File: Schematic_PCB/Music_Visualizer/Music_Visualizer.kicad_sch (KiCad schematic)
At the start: 145 parts, among them J1 AudioJack3, J3 Screw_Terminal_01x02, SW1 SW_SPDT, U1 LM324, U2 LM324, U3 LM324, U4 LM324, U5 LM324, U6 LM324, U7 LM324

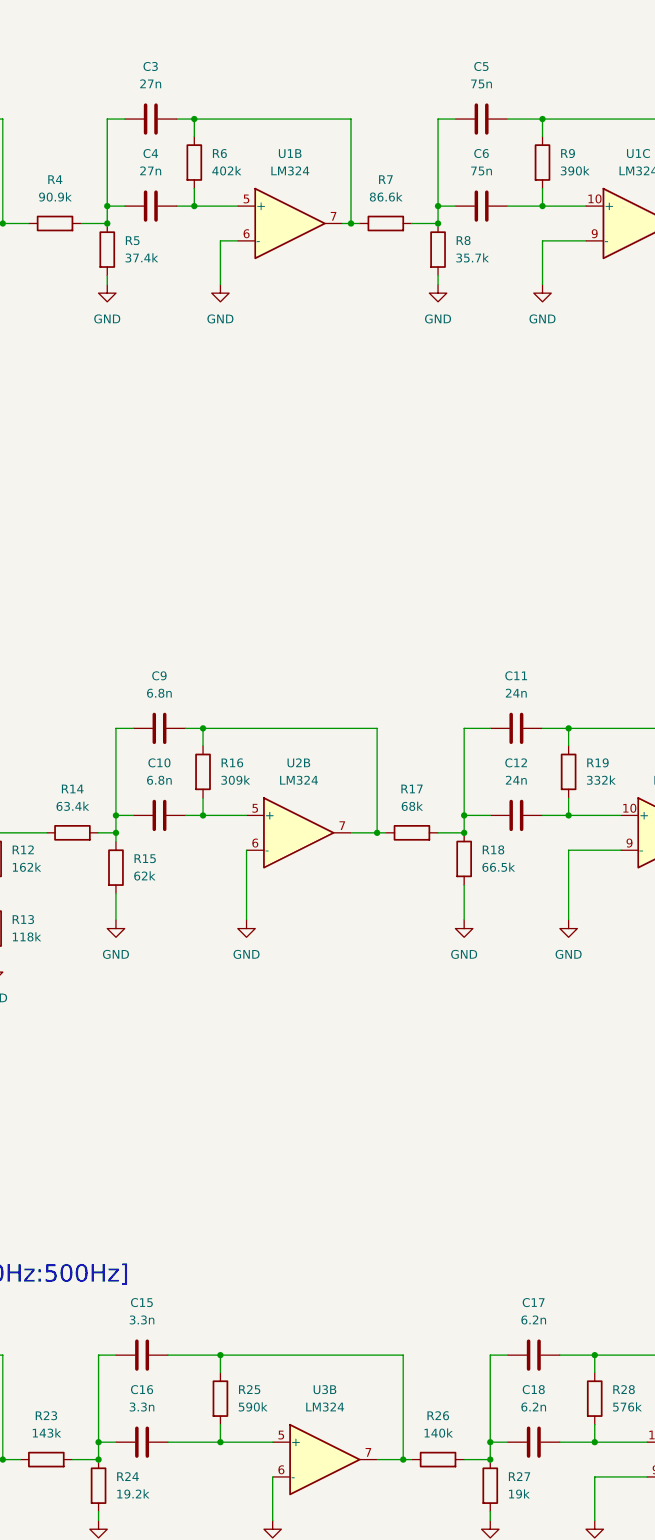
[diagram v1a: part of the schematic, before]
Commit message: Started sourcing parts from digikey, got to part 15, corrected mistakes as I go along
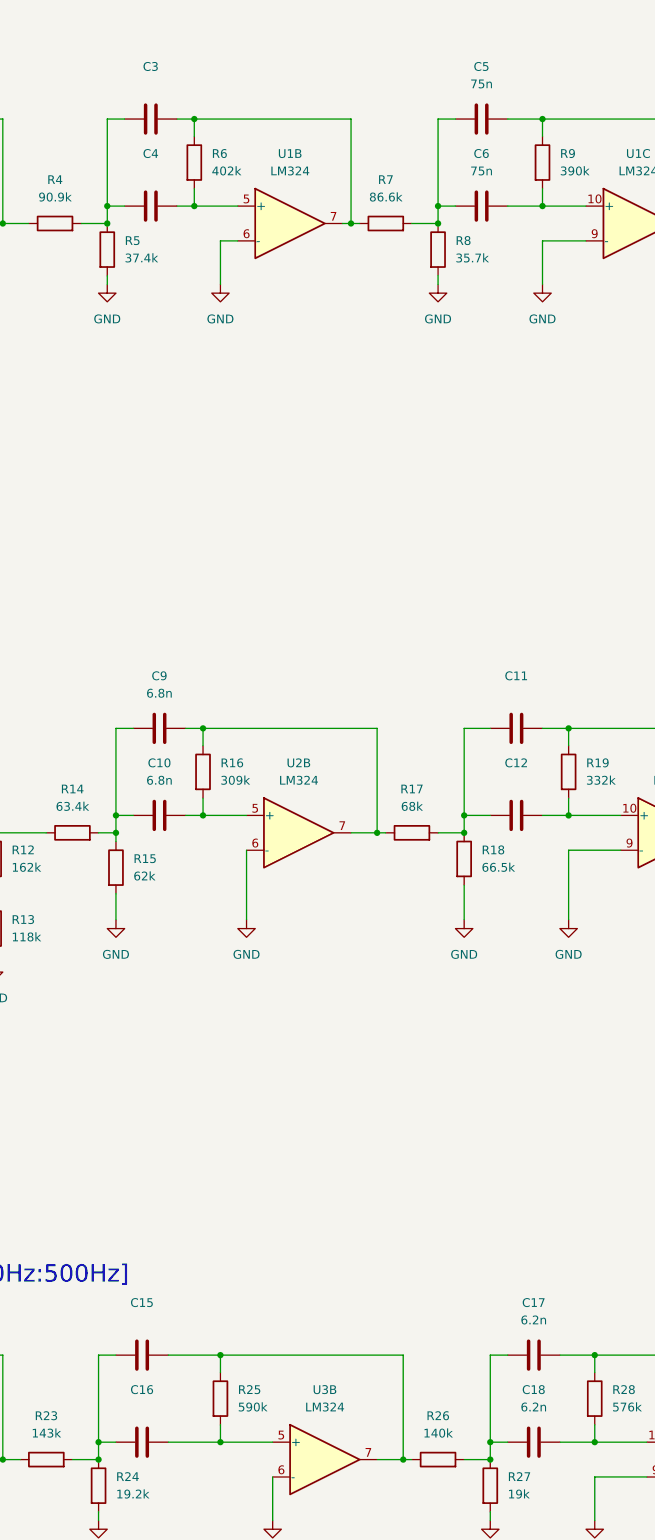
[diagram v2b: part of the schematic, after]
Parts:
- C11, C12: value 24n -> (none); footprint Capacitor_SMD:C_1206_3216Metric -> (none)
- C15, C16: value 3.3n -> (none); footprint Capacitor_SMD:C_0402_1005Metric -> (none)
- C3, C4: value 27n -> (none); footprint Capacitor_SMD:C_0402_1005Metric -> (none)
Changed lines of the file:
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@@
     (in_bom yes) (on_board yes) (fields_autoplaced)
     (property "Reference" "C11" (id 0) (at 189.23 116.84 90))
-    (property "Value" "24n" (id 1) (at 189.23 119.38 90))
-    (property "Footprint" "Capacitor_SMD:C_1206_3216Metric" (id 2) (at 193.04 123.4948 0)
+    (property "Value" "" (id 1) (at 189.23 119.38 90))
+    (property "Footprint" "" (id 2) (at 193.04 123.4948 0)
       (effects (font (size 1.27 1.27)) hide)
     )
@@
     (in_bom yes) (on_board yes) (fields_autoplaced)
     (property "Reference" "C12" (id 0) (at 189.23 129.54 90))
-    (property "Value" "24n" (id 1) (at 189.23 132.08 90))
-    (property "Footprint" "Capacitor_SMD:C_1206_3216Metric" (id 2) (at 193.04 136.1948 0)
+    (property "Value" "" (id 1) (at 189.23 132.08 90))
+    (property "Footprint" "" (id 2) (at 193.04 136.1948 0)
       (effects (font (size 1.27 1.27)) hide)
     )
@@
     (in_bom yes) (on_board yes) (fields_autoplaced)
     (property "Reference" "C15" (id 0) (at 134.62 208.28 90))
-    (property "Value" "3.3n" (id 1) (at 134.62 210.82 90))
-    (property "Footprint" "Capacitor_SMD:C_0402_1005Metric" (id 2) (at 138.43 214.9348 0)
+    (property "Value" "" (id 1) (at 134.62 210.82 90))
+    (property "Footprint" "" (id 2) (at 138.43 214.9348 0)
       (effects (font (size 1.27 1.27)) hide)
     )
@@
     (in_bom yes) (on_board yes) (fields_autoplaced)
     (property "Reference" "C4" (id 0) (at 135.89 40.64 90))
-    (property "Value" "27n" (id 1) (at 135.89 43.18 90))
-    (property "Footprint" "Capacitor_SMD:C_0402_1005Metric" (id 2) (at 139.7 47.2948 0)
+    (property "Value" "" (id 1) (at 135.89 43.18 90))
+    (property "Footprint" "" (id 2) (at 139.7 47.2948 0)
       (effects (font (size 1.27 1.27)) hide)
     )
@@
     (in_bom yes) (on_board yes)
     (property "Reference" "C3" (id 0) (at 135.89 27.94 90))
-    (property "Value" "27n" (id 1) (at 135.89 30.48 90))
-    (property "Footprint" "Capacitor_SMD:C_0402_1005Metric" (id 2) (at 139.7 34.5948 0)
+    (property "Value" "" (id 1) (at 135.89 30.48 90))
+    (property "Footprint" "" (id 2) (at 139.7 34.5948 0)
       (effects (font (size 1.27 1.27)) hide)
     )
@@
     (in_bom yes) (on_board yes) (fields_autoplaced)
     (property "Reference" "C16" (id 0) (at 134.62 220.98 90))
-    (property "Value" "3.3n" (id 1) (at 134.62 223.52 90))
-    (property "Footprint" "Capacitor_SMD:C_0402_1005Metric" (id 2) (at 138.43 227.6348 0)
+    (property "Value" "" (id 1) (at 134.62 223.52 90))
+    (property "Footprint" "" (id 2) (at 138.43 227.6348 0)
       (effects (font (size 1.27 1.27)) hide)
     )
@@
     )
     (path "/9bf0cba7-9517-4cba-992a-c8ed29af4729"
-      (reference "C3") (unit 1) (value "27n") (footprint "Capacitor_SMD:C_0402_1005Metric")
+      (reference "C3") (unit 1) (value "27n") (footprint "Capacitor_SMD:C_0603_1608Metric")
     )
     (path "/8c47b6ff-34b1-402d-a1f0-32ec90f1ac1e"
-      (reference "C4") (unit 1) (value "27n") (footprint "Capacitor_SMD:C_0402_1005Metric")
+      (reference "C4") (unit 1) (value "27n") (footprint "Capacitor_SMD:C_0603_1608Metric")
     )
     (path "/77886ef4-a79a-47d1-b490-9ff1ad540d06"
@@
     )
     (path "/090684f0-2db5-4c27-adcd-136c105cb53b"
-      (reference "C11") (unit 1) (value "24n") (footprint "Capacitor_SMD:C_1206_3216Metric")
+      (reference "C11") (unit 1) (value "24n") (footprint "Capacitor_SMD:C_0805_2012Metric")
     )
     (path "/2a2a8a1f-a295-45d5-9418-ae650bcb2e29"
-      (reference "C12") (unit 1) (value "24n") (footprint "Capacitor_SMD:C_1206_3216Metric")
+      (reference "C12") (unit 1) (value "24n") (footprint "Capacitor_SMD:C_0805_2012Metric")
     )
     (path "/20700322-fdbb-423a-a695-59bcf586eb75"
@@
     )
     (path "/79e9dcc8-186f-4c45-a5c4-64194af1b0b7"
-      (reference "C15") (unit 1) (value "3.3n") (footprint "Capacitor_SMD:C_0402_1005Metric")
+      (reference "C15") (unit 1) (value "3.3n") (footprint "Capacitor_SMD:C_0201_0603Metric")
     )
     (path "/fa3632db-5db7-41c9-81a2-0fd4b3e31b83"
-      (reference "C16") (unit 1) (value "3.3n") (footprint "Capacitor_SMD:C_0402_1005Metric")
+      (reference "C16") (unit 1) (value "3.3n") (footprint "Capacitor_SMD:C_0201_0603Metric")
     )
     (path "/35d17c18-0872-4b14-af92-9b4e4ed99599"

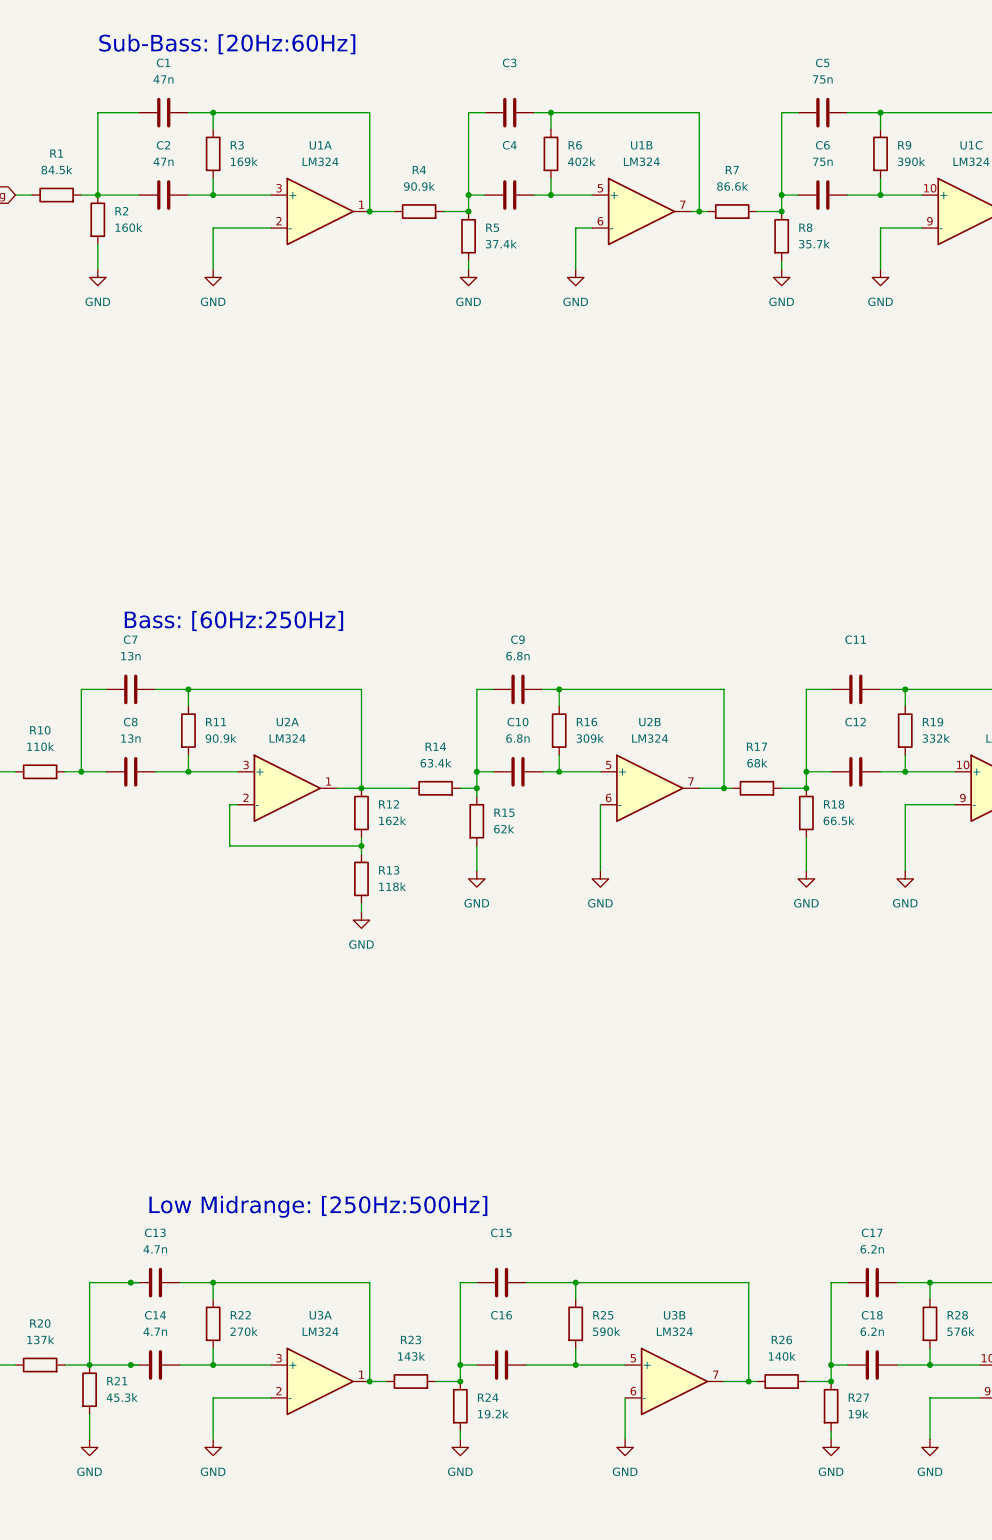
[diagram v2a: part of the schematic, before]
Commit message: Finished digi-key BOM and made appropriate changes to schematic and PCB
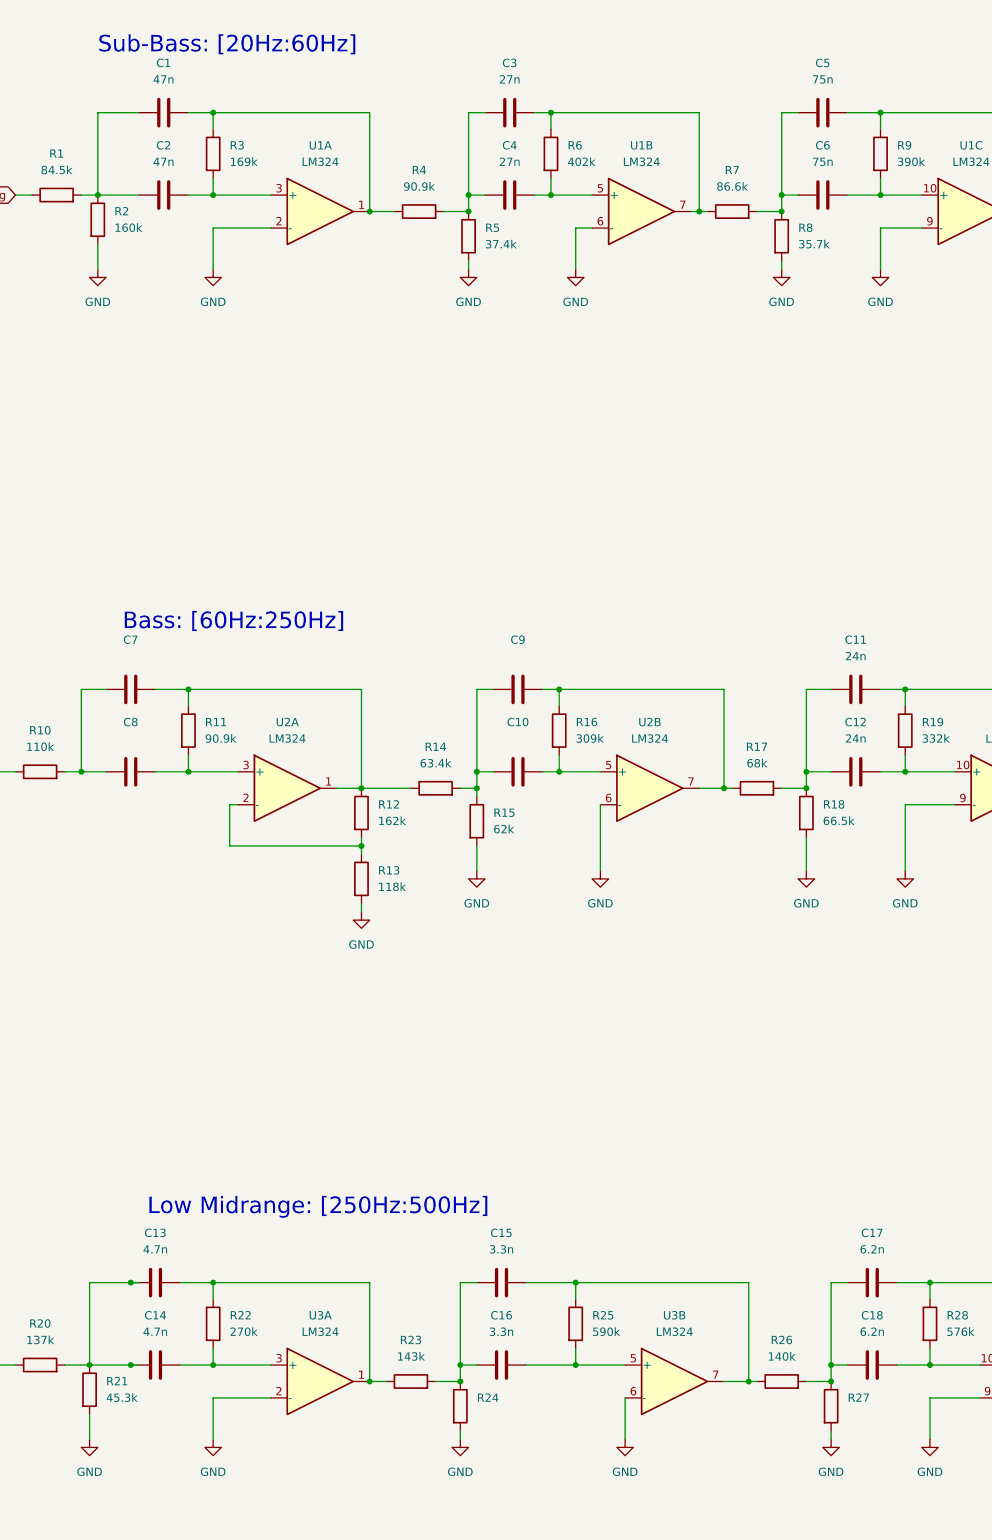
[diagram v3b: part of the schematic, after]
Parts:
- C10, C9: value 6.8n -> (none); footprint Capacitor_SMD:C_0201_0603Metric -> (none)
- C11, C12: value (none) -> 24n; footprint (none) -> Capacitor_SMD:C_0805_2012Metric
- C15, C16: value (none) -> 3.3n; footprint (none) -> Capacitor_SMD:C_0201_0603Metric
- C3, C4: value (none) -> 27n; footprint (none) -> Capacitor_SMD:C_0603_1608Metric
- C7, C8: value 13n -> (none); footprint Capacitor_SMD:C_0402_1005Metric -> (none)
- R24: value 19.2k -> (none)
- R27: value 19k -> (none)
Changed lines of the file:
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@@
     (in_bom yes) (on_board yes) (fields_autoplaced)
     (property "Reference" "C7" (id 0) (at 77.47 116.84 90))
-    (property "Value" "13n" (id 1) (at 77.47 119.38 90))
-    (property "Footprint" "Capacitor_SMD:C_0402_1005Metric" (id 2) (at 81.28 123.4948 0)
+    (property "Value" "" (id 1) (at 77.47 119.38 90))
+    (property "Footprint" "" (id 2) (at 81.28 123.4948 0)
       (effects (font (size 1.27 1.27)) hide)
     )
@@
     (in_bom yes) (on_board yes) (fields_autoplaced)
     (property "Reference" "C11" (id 0) (at 189.23 116.84 90))
-    (property "Value" "" (id 1) (at 189.23 119.38 90))
-    (property "Footprint" "" (id 2) (at 193.04 123.4948 0)
+    (property "Value" "24n" (id 1) (at 189.23 119.38 90))
+    (property "Footprint" "Capacitor_SMD:C_0805_2012Metric" (id 2) (at 193.04 123.4948 0)
       (effects (font (size 1.27 1.27)) hide)
     )
@@
       (effects (font (size 1.27 1.27)) (justify left))
     )
-    (property "Value" "19.2k" (id 1) (at 130.81 236.2199 0)
+    (property "Value" "" (id 1) (at 130.81 236.2199 0)
       (effects (font (size 1.27 1.27)) (justify left))
     )
@@
     (in_bom yes) (on_board yes) (fields_autoplaced)
     (property "Reference" "C12" (id 0) (at 189.23 129.54 90))
-    (property "Value" "" (id 1) (at 189.23 132.08 90))
-    (property "Footprint" "" (id 2) (at 193.04 136.1948 0)
+    (property "Value" "24n" (id 1) (at 189.23 132.08 90))
+    (property "Footprint" "Capacitor_SMD:C_0805_2012Metric" (id 2) (at 193.04 136.1948 0)
       (effects (font (size 1.27 1.27)) hide)
     )
@@
     (in_bom yes) (on_board yes) (fields_autoplaced)
     (property "Reference" "C10" (id 0) (at 137.16 129.54 90))
-    (property "Value" "6.8n" (id 1) (at 137.16 132.08 90))
-    (property "Footprint" "Capacitor_SMD:C_0201_0603Metric" (id 2) (at 140.97 136.1948 0)
+    (property "Value" "" (id 1) (at 137.16 132.08 90))
+    (property "Footprint" "" (id 2) (at 140.97 136.1948 0)
       (effects (font (size 1.27 1.27)) hide)
     )
@@
     (in_bom yes) (on_board yes) (fields_autoplaced)
     (property "Reference" "C15" (id 0) (at 134.62 208.28 90))
-    (property "Value" "" (id 1) (at 134.62 210.82 90))
-    (property "Footprint" "" (id 2) (at 138.43 214.9348 0)
+    (property "Value" "3.3n" (id 1) (at 134.62 210.82 90))
+    (property "Footprint" "Capacitor_SMD:C_0201_0603Metric" (id 2) (at 138.43 214.9348 0)
       (effects (font (size 1.27 1.27)) hide)
     )
@@
     (in_bom yes) (on_board yes) (fields_autoplaced)
     (property "Reference" "C9" (id 0) (at 137.16 116.84 90))
-    (property "Value" "6.8n" (id 1) (at 137.16 119.38 90))
-    (property "Footprint" "Capacitor_SMD:C_0201_0603Metric" (id 2) (at 140.97 123.4948 0)
+    (property "Value" "" (id 1) (at 137.16 119.38 90))
+    (property "Footprint" "" (id 2) (at 140.97 123.4948 0)
       (effects (font (size 1.27 1.27)) hide)
     )
@@
     (in_bom yes) (on_board yes) (fields_autoplaced)
     (property "Reference" "C4" (id 0) (at 135.89 40.64 90))
-    (property "Value" "" (id 1) (at 135.89 43.18 90))
-    (property "Footprint" "" (id 2) (at 139.7 47.2948 0)
+    (property "Value" "27n" (id 1) (at 135.89 43.18 90))
+    (property "Footprint" "Capacitor_SMD:C_0603_1608Metric" (id 2) (at 139.7 47.2948 0)
       (effects (font (size 1.27 1.27)) hide)
     )
@@
     (in_bom yes) (on_board yes)
     (property "Reference" "C3" (id 0) (at 135.89 27.94 90))
-    (property "Value" "" (id 1) (at 135.89 30.48 90))
-    (property "Footprint" "" (id 2) (at 139.7 34.5948 0)
+    (property "Value" "27n" (id 1) (at 135.89 30.48 90))
+    (property "Footprint" "Capacitor_SMD:C_0603_1608Metric" (id 2) (at 139.7 34.5948 0)
       (effects (font (size 1.27 1.27)) hide)
     )
@@
       (effects (font (size 1.27 1.27)) (justify left))
     )
-    (property "Value" "19k" (id 1) (at 187.96 236.2199 0)
+    (property "Value" "" (id 1) (at 187.96 236.2199 0)
       (effects (font (size 1.27 1.27)) (justify left))
     )
@@
     (in_bom yes) (on_board yes) (fields_autoplaced)
     (property "Reference" "C8" (id 0) (at 77.47 129.54 90))
-    (property "Value" "13n" (id 1) (at 77.47 132.08 90))
-    (property "Footprint" "Capacitor_SMD:C_0402_1005Metric" (id 2) (at 81.28 136.1948 0)
+    (property "Value" "" (id 1) (at 77.47 132.08 90))
+    (property "Footprint" "" (id 2) (at 81.28 136.1948 0)
       (effects (font (size 1.27 1.27)) hide)
     )
@@
     (in_bom yes) (on_board yes) (fields_autoplaced)
     (property "Reference" "C16" (id 0) (at 134.62 220.98 90))
-    (property "Value" "" (id 1) (at 134.62 223.52 90))
-    (property "Footprint" "" (id 2) (at 138.43 227.6348 0)
+    (property "Value" "3.3n" (id 1) (at 134.62 223.52 90))
+    (property "Footprint" "Capacitor_SMD:C_0201_0603Metric" (id 2) (at 138.43 227.6348 0)
       (effects (font (size 1.27 1.27)) hide)
     )
@@
     )
     (path "/07ee7e0f-2985-4d61-9b50-269fb321160d"
-      (reference "C7") (unit 1) (value "13n") (footprint "Capacitor_SMD:C_0402_1005Metric")
+      (reference "C7") (unit 1) (value "13n") (footprint "Capacitor_SMD:C_0805_2012Metric")
     )
     (path "/f487e740-61ea-48e8-a052-40ab7e8322a0"
-      (reference "C8") (unit 1) (value "13n") (footprint "Capacitor_SMD:C_0402_1005Metric")
+      (reference "C8") (unit 1) (value "13n") (footprint "Capacitor_SMD:C_0805_2012Metric")
     )
     (path "/83d23cec-73ff-46df-90f0-af0a3e52ad46"
-      (reference "C9") (unit 1) (value "6.8n") (footprint "Capacitor_SMD:C_0201_0603Metric")
+      (reference "C9") (unit 1) (value "6.8n") (footprint "Capacitor_SMD:C_0805_2012Metric")
     )
     (path "/671fc4a8-8b88-4bcb-9c54-7c1fba0aad0e"
-      (reference "C10") (unit 1) (value "6.8n") (footprint "Capacitor_SMD:C_0201_0603Metric")
+      (reference "C10") (unit 1) (value "6.8n") (footprint "Capacitor_SMD:C_0805_2012Metric")
     )
     (path "/090684f0-2db5-4c27-adcd-136c105cb53b"
@@
     )
     (path "/24620dcc-52e7-4176-bbe7-843dfe8a0615"
-      (reference "R24") (unit 1) (value "19.2k") (footprint "Resistor_SMD:R_0201_0603Metric")
+      (reference "R24") (unit 1) (value "19.1k") (footprint "Resistor_SMD:R_0201_0603Metric")
     )
     (path "/d4ca4118-2e3c-4333-8a48-cfd796f4e144"
@@
     )
     (path "/b7849076-c46e-483f-8c49-48d7f45f5cd4"
-      (reference "R27") (unit 1) (value "19k") (footprint "Resistor_SMD:R_0201_0603Metric")
+      (reference "R27") (unit 1) (value "18.7k") (footprint "Resistor_SMD:R_0201_0603Metric")
     )
     (path "/de842ede-51e6-49b2-8854-cc04ffd37056"
